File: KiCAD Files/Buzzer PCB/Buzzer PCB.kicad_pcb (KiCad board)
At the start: 2 copper layers, 25.2 x 22.9 mm, 13 parts, among them J1 JST-PH Battery IN, J2 JST-PH Feather BAT OUT, J4 Feather D13, Q1 S8050, SW1 SS12D00G5

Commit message: V2 PCB done
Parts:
- C1: value 47-100uF -> 47-100uF ELEC
- C2: value 0.1uF -> 0.1uF CER
- J1, J2: footprint Connector_JST:JST_PH_S2B-PH-K_1x02_P2.00mm_Horizontal -> Connector_JST:JST_PH_B2B-PH-K_1x02_P2.00mm_Vertical
- moved SW1 2.08 mm to (105.9, 104.9)
- moved D1 1.71 mm to (90.8, 112.4)
- moved C2 1.56 mm to (105.7, 98.4)
- moved J1 1.49 mm to (94.5, 95.6), turned to 180 degrees
- moved J2 1.14 mm to (100.7, 95.6), turned to 180 degrees
- moved C1 0.78 mm to (101.4, 111.2), turned to 180 degrees
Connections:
- J1 pad 1: BAT_IN -> GND
- J1 pad 2: GND -> BAT_IN
- J2 pad 1: SW_BAT -> GND
- J2 pad 2: GND -> SW_BAT
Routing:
- net GND: track 63.1 -> 56.5 mm
- net BAT_IN: track 20.1 -> 17.6 mm
- net BUZZER_LOW: track 12.7 -> 13.4 mm

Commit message: two_sided
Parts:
- J1, J2: footprint Connector_JST:JST_PH_B2B-PH-K_1x02_P2.00mm_Vertical -> Connector_JST:JST_PH_S2B-PH-K_1x02_P2.00mm_Horizontal
- moved J4 31.3 mm to (107.0, 116.0), turned to 180 degrees
- moved H1 30.1 mm to (85.4, 114.7), turned to 180 degrees
- moved H2 26.7 mm to (85.4, 96.9), turned to 180 degrees
- moved R1 24.0 mm to (106.9, 110.3), turned to 90 degrees
- moved C2 22.1 mm to (87.2, 110.4), turned to 0 degrees
- moved R2 19.8 mm to (104.4, 110.3), turned to -90 degrees
- moved D1 19.6 mm to (102.1, 96.4), turned to 0 degrees
- moved SW1 19.0 mm to (87.0, 103.9), turned to 90 degrees
- moved J2 18.7 mm to (93.2, 112.7), turned to 0 degrees
- moved J1 17.8 mm to (99.4, 112.7), turned to 0 degrees
- moved Q1 17.8 mm to (104.9, 101.6), turned to 90 degrees
- moved C1 16.8 mm to (91.5, 97.6), turned to 0 degrees
- moved BZ1 0.71 mm to (96.9, 104.1), turned to 0 degrees
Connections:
- J1 pad 1: GND -> BAT_IN
- J1 pad 2: BAT_IN -> GND
- J2 pad 1: GND -> SW_BAT
- J2 pad 2: SW_BAT -> GND
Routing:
- net D13: track 1.90 -> 6.42 mm, vias 0 -> 1
- net SW_BAT: track 48.2 -> 44.5 mm
- net BAT_IN: track 17.6 -> 14.4 mm
- net GND: track 56.5 -> 59.0 mm
- net BUZZER_LOW: track 13.4 -> 12.7 mm
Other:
- outline, holes or cut-outs redrawn

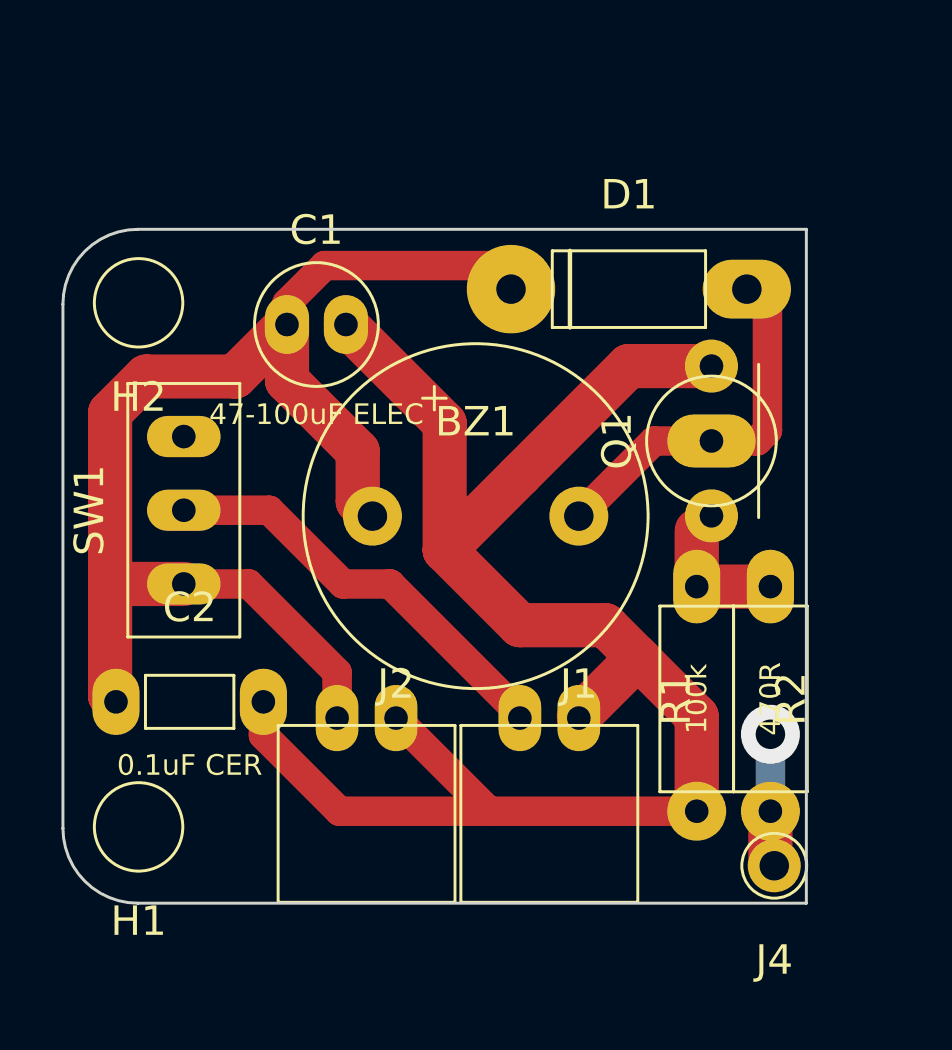
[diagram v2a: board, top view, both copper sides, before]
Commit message: Fix S8050 pinout and buzzer test interval
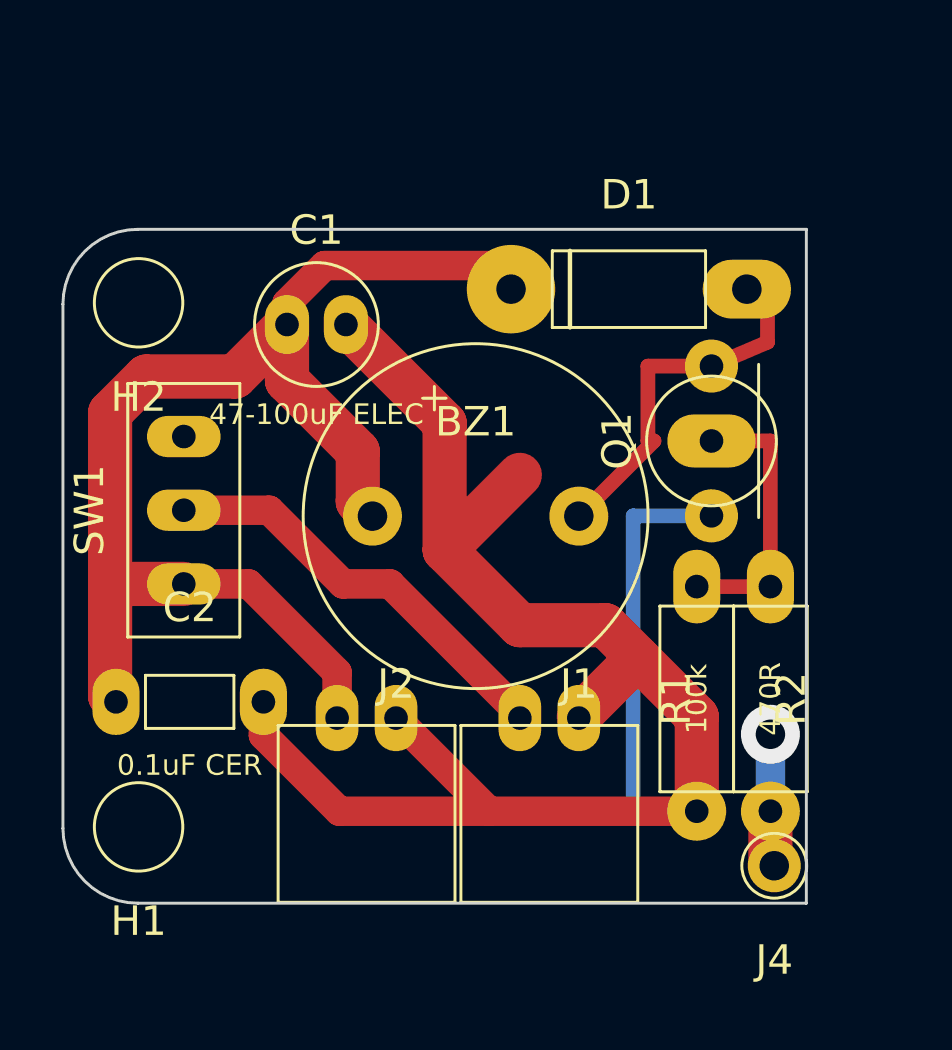
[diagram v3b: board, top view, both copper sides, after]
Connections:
- Q1 pad 1: BUZZER_BASE -> GND
- Q1 pad 2: BUZZER_LOW -> BUZZER_BASE
- Q1 pad 3: GND -> BUZZER_LOW
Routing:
- net GND: track 59.0 -> 65.8 mm
- net BUZZER_BASE: track 5.11 -> 9.44 mm
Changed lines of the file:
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@@
 		(layer "F.Cu")
 		(at 104.856051 101.563949 90)
-		(descr "S8050 NPN TO-92, formed leads, 2.54mm pad pitch, BCE per schematic, 0.8mm drills")
+		(descr "S8050 NPN TO-92, formed leads, 2.54mm pad pitch, EBC pinout, 0.8mm drills")
 		(property "Reference" "Q1"
 			(at 0 -3.2 90)
@@
 			)
 		)
-		(property "Description" "S8050 NPN TO-92, formed leads, 2.54mm pad pitch, BCE per schematic, 0.8mm drills"
+		(property "Description" "S8050 NPN TO-92, formed leads, 2.54mm pad pitch, EBC pinout, 0.8mm drills"
 			(at 0 0 90)
 			(layer "F.Fab")
@@
 			(keep_end_layers no)
 			(zone_layer_connections)
-			(net "BUZZER_BASE")
-			(pinfunction "B")
+			(net "GND")
+			(pinfunction "E")
 			(pintype "passive")
 		)
@@
 			(keep_end_layers no)
 			(zone_layer_connections)
-			(net "BUZZER_LOW")
-			(pinfunction "C")
+			(net "BUZZER_BASE")
+			(pinfunction "B")
 			(pintype "passive")
 		)
@@
 			(keep_end_layers no)
 			(zone_layer_connections)
-			(net "GND")
-			(pinfunction "E")
+			(net "BUZZER_LOW")
+			(pinfunction "C")
 			(pintype "passive")
 		)
@@
 	)
 	(segment
-		(start 102.046051 99.023949)
-		(end 104.856051 99.023949)
-		(width 1.5)
-		(layer "F.Cu")
+		(start 104.856051 104.103949)
+		(end 102.2 104.103949)
+		(width 0.5)
+		(layer "B.Cu")
+		(net "GND")
+	)
+	(segment
+		(start 102.2 104.103949)
+		(end 102.2 114.123949)
+		(width 0.5)
+		(layer "B.Cu")
+		(net "GND")
+	)
+	(segment
+		(start 102.2 114.123949)
+		(end 104.356051 114.123949)
+		(width 0.5)
+		(layer "B.Cu")
 		(net "GND")
 	)
@@
 	)
 	(segment
-		(start 98.356051 102.713949)
-		(end 102.046051 99.023949)
-		(width 1.5)
-		(layer "F.Cu")
-		(net "GND")
-	)
-	(segment
-		(start 104.356051 106.503949)
-		(end 104.356051 104.603949)
-		(width 1.5)
+		(start 106.856051 106.503949)
+		(end 106.856051 101.563949)
+		(width 0.5)
 		(layer "F.Cu")
 		(net "BUZZER_BASE")
 	)
 	(segment
-		(start 104.356051 104.603949)
-		(end 104.856051 104.103949)
-		(width 1)
+		(start 106.856051 101.563949)
+		(end 104.856051 101.563949)
+		(width 0.5)
 		(layer "F.Cu")
 		(net "BUZZER_BASE")
@@
 		(start 106.856051 106.503949)
 		(end 104.356051 106.503949)
-		(width 1.5)
+		(width 0.5)
 		(layer "F.Cu")
 		(net "BUZZER_BASE")
@@
 	)
 	(segment
-		(start 106.406051 101.563949)
-		(end 104.856051 101.563949)
-		(width 1)
-		(layer "F.Cu")
-		(net "BUZZER_LOW")
-	)
-	(segment
 		(start 106.756051 97.113949)
-		(end 106.756051 101.213949)
-		(width 1)
+		(end 106.756051 98.213949)
+		(width 0.5)
 		(layer "F.Cu")
 		(net "BUZZER_LOW")
@@
 		(start 102.906051 101.563949)
 		(end 100.356051 104.113949)
-		(width 1)
+		(width 0.5)
 		(layer "F.Cu")
 		(net "BUZZER_LOW")
 	)
 	(segment
-		(start 104.856051 101.563949)
+		(start 104.856051 99.023949)
+		(end 102.7 99.023949)
+		(width 0.5)
+		(layer "F.Cu")
+		(net "BUZZER_LOW")
+	)
+	(segment
+		(start 102.7 99.023949)
+		(end 102.7 101.563949)
+		(width 0.5)
+		(layer "F.Cu")
+		(net "BUZZER_LOW")
+	)
+	(segment
+		(start 102.7 101.563949)
 		(end 102.906051 101.563949)
-		(width 1)
+		(width 0.5)
 		(layer "F.Cu")
 		(net "BUZZER_LOW")
@@
 		(start 106.056051 96.413949)
 		(end 106.756051 97.113949)
-		(width 1)
+		(width 0.5)
 		(layer "F.Cu")
 		(net "BUZZER_LOW")
 	)
 	(segment
-		(start 106.756051 101.213949)
-		(end 106.406051 101.563949)
-		(width 1)
+		(start 106.756051 98.213949)
+		(end 104.856051 99.023949)
+		(width 0.5)
 		(layer "F.Cu")
 		(net "BUZZER_LOW")

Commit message: Fixed transistor pins
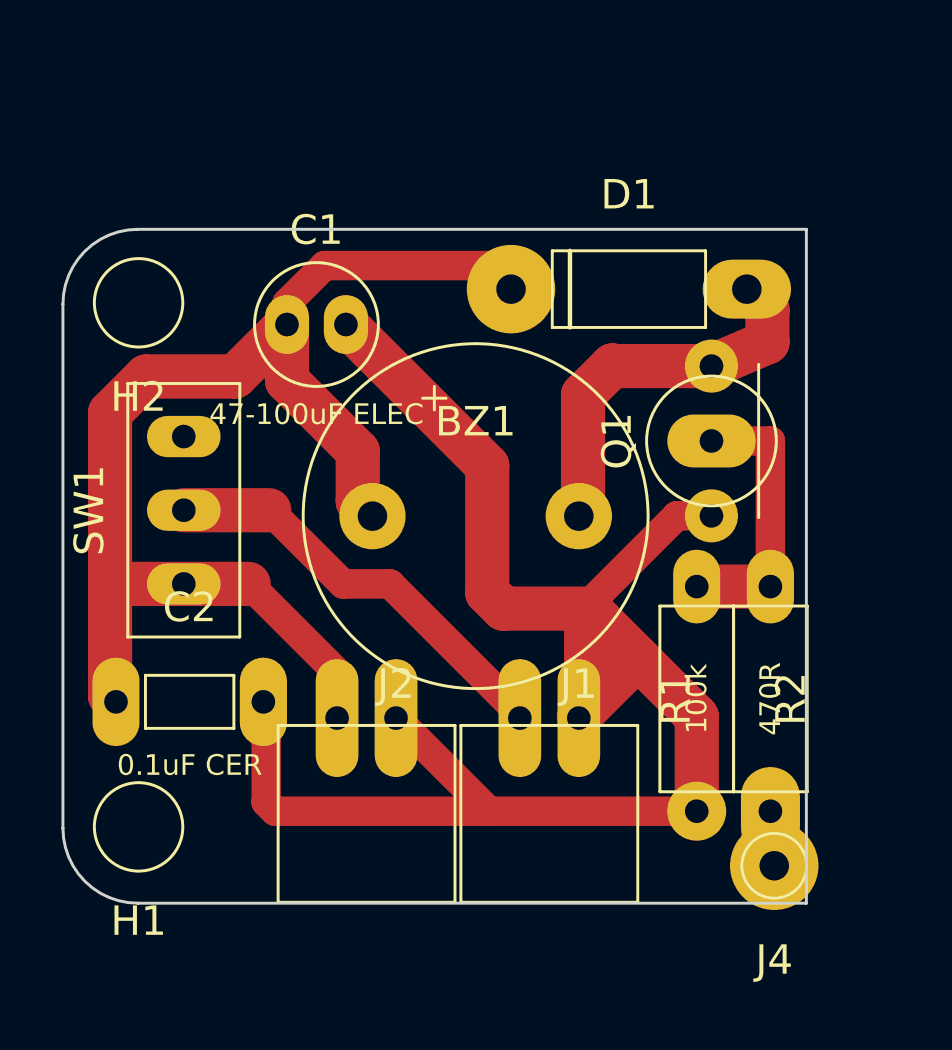
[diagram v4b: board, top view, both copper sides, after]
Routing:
- net GND: track 65.8 -> 59.8 mm
- net D13: track 6.42 -> 3.81 mm, vias 1 -> 0
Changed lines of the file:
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@@
 		(capping no)
 		(filling no)
-		(aux_axis_origin 85.422051 114.655349)
+		(aux_axis_origin 78.1 122.3)
 		(pcbplotparams
 			(layerselection 0x00000000_00000000_55555555_57555555)
@@
 			(layer "F.Fab")
 		)
-		(pad "1" thru_hole circle
+		(pad "e" thru_hole oval
 			(at 0 0 180)
-			(size 1.8 1.8)
+			(size 3 3)
 			(drill 1)
 			(layers "*.Cu" "F.Mask")
@@
 		(pad "1" thru_hole oval
 			(at -2.5 0)
-			(size 1.6 2.25)
+			(size 1.6 3)
 			(drill 0.8)
 			(layers "*.Cu" "F.Mask")
@@
 		(pad "2" thru_hole oval
 			(at 2.5 0)
-			(size 1.6 2.25)
+			(size 1.6 3)
 			(drill 0.8)
 			(layers "*.Cu" "F.Mask")
@@
 		(pad "1" thru_hole oval
 			(at -1 -1.75)
-			(size 1.45 2.25)
+			(size 1.45 4)
 			(drill 0.8)
 			(layers "*.Cu" "F.Mask")
@@
 		(pad "2" thru_hole oval
 			(at 1 -1.75)
-			(size 1.45 2.25)
+			(size 1.45 4)
 			(drill 0.8)
 			(layers "*.Cu" "F.Mask")
@@
 		(pad "1" thru_hole oval
 			(at -1 -1.75)
-			(size 1.45 2.25)
+			(size 1.45 4)
 			(drill 0.8)
 			(layers "*.Cu" "F.Mask")
@@
 		(pad "2" thru_hole oval
 			(at 1 -1.75)
-			(size 1.45 2.25)
+			(size 1.45 4)
 			(drill 0.8)
 			(layers "*.Cu" "F.Mask")
@@
 			(layer "F.Fab")
 		)
-		(pad "1" thru_hole circle
+		(pad "1" thru_hole oval
 			(at -3.81 0 90)
-			(size 2 2)
+			(size 3 2)
 			(drill 0.8)
 			(layers "*.Cu" "F.Mask")
@@
 		(pad "1" thru_hole circle
 			(at -3.5 0)
-			(size 2 2)
+			(size 2.25 2.25)
 			(drill 1)
 			(layers "*.Cu" "F.Mask")
@@
 		(pad "2" thru_hole circle
 			(at 3.5 0)
-			(size 2 2)
+			(size 2.25 2.25)
 			(drill 1)
 			(layers "*.Cu" "F.Mask")
@@
 		(start 106.856051 114.123949)
 		(end 106.856051 115.843949)
-		(width 1.5)
+		(width 2)
 		(layer "F.Cu")
 		(net "D13")
@@
 		(net "D13")
 	)
-	(via
-		(at 106.856051 111.513949)
-		(size 2)
-		(drill 1)
-		(layers "F.Cu" "B.Cu")
-		(free yes)
-		(net "D13")
-	)
 	(segment
 		(start 106.986051 114.253949)
@@
 	)
 	(segment
-		(start 106.856051 114.123949)
-		(end 106.856051 111.513949)
+		(start 106.986051 115.973949)
+		(end 106.986051 114.253949)
 		(width 1)
 		(layer "B.Cu")
@@
 	)
 	(segment
-		(start 106.986051 115.973949)
-		(end 106.986051 114.253949)
-		(width 1)
-		(layer "B.Cu")
-		(net "D13")
-	)
-	(segment
 		(start 91.731177 95.613949)
 		(end 90.456051 96.889075)
@@
 		(start 89.156051 106.413949)
 		(end 86.956051 106.413949)
-		(width 1)
+		(width 1.5)
 		(layer "F.Cu")
 		(net "SW_BAT")
@@
 	)
 	(segment
-		(start 98.356051 107.813949)
-		(end 95.806051 105.263949)
-		(width 1.5)
+		(start 92.456051 97.613949)
+		(end 97.25 102.407898)
+		(width 1.5)
+		(layer "F.Cu")
+		(net "GND")
+	)
+	(segment
+		(start 89.656051 111.545319)
+		(end 89.75 111.639268)
+		(width 1)
+		(layer "F.Cu")
+		(net "GND")
+	)
+	(segment
+		(start 100.692102 107.089873)
+		(end 100.692102 107.25)
+		(width 1)
 		(layer "F.Cu")
 		(net "GND")
@@
 	)
 	(segment
-		(start 102.356051 108.913949)
-		(end 101.256051 107.813949)
-		(width 1.5)
-		(layer "F.Cu")
-		(net "GND")
-	)
-	(segment
-		(start 100.356051 110.913949)
+		(start 100.692102 107.25)
 		(end 102.356051 108.913949)
 		(width 1.5)
@@
 	)
 	(segment
-		(start 95.806051 105.263949)
-		(end 98.356051 102.713949)
-		(width 1.5)
+		(start 89.75 113.819634)
+		(end 90.054315 114.123949)
+		(width 1)
+		(layer "F.Cu")
+		(net "GND")
+	)
+	(segment
+		(start 100.356051 107.586051)
+		(end 100.356051 108.75)
+		(width 1)
+		(layer "F.Cu")
+		(net "GND")
+	)
+	(segment
+		(start 89.75 111.639268)
+		(end 89.75 113.819634)
+		(width 1)
+		(layer "F.Cu")
+		(net "GND")
+	)
+	(segment
+		(start 100.692102 107.25)
+		(end 100.356051 107.586051)
+		(width 1)
+		(layer "F.Cu")
+		(net "GND")
+	)
+	(segment
+		(start 97.25 102.407898)
+		(end 97.25 106.707898)
+		(width 1.5)
+		(layer "F.Cu")
+		(net "GND")
+	)
+	(segment
+		(start 97.25 106.707898)
+		(end 97.792102 107.25)
+		(width 1.5)
+		(layer "F.Cu")
+		(net "GND")
+	)
+	(segment
+		(start 101.76 109.51)
+		(end 102.356051 108.913949)
+		(width 1.5)
+		(layer "F.Cu")
+		(net "GND")
+	)
+	(segment
+		(start 100.356051 108.75)
+		(end 101 108.75)
+		(width 1)
 		(layer "F.Cu")
 		(net "GND")
@@
 	)
 	(segment
+		(start 94.156051 110.963949)
+		(end 97.316051 114.123949)
+		(width 1)
+		(layer "F.Cu")
+		(net "GND")
+	)
+	(segment
+		(start 104.356051 114.123949)
+		(end 104.356051 110.913949)
+		(width 1.5)
+		(layer "F.Cu")
+		(net "GND")
+	)
+	(segment
+		(start 100.356051 108.75)
+		(end 100.356051 110.963949)
+		(width 1)
+		(layer "F.Cu")
+		(net "GND")
+	)
+	(segment
+		(start 90.054315 114.123949)
+		(end 97.316051 114.123949)
+		(width 1)
+		(layer "F.Cu")
+		(net "GND")
+	)
+	(segment
+		(start 101 108.75)
+		(end 101.76 109.51)
+		(width 1)
+		(layer "F.Cu")
+		(net "GND")
+	)
+	(segment
+		(start 103.678026 104.103949)
+		(end 100.692102 107.089873)
+		(width 1)
+		(layer "F.Cu")
+		(net "GND")
+	)
+	(segment
+		(start 97.792102 107.25)
+		(end 100.692102 107.25)
+		(width 1.5)
+		(layer "F.Cu")
+		(net "GND")
+	)
+	(segment
+		(start 104.856051 104.103949)
+		(end 103.678026 104.103949)
+		(width 1)
+		(layer "F.Cu")
+		(net "GND")
+	)
+	(segment
+		(start 100.356051 110.913949)
+		(end 101.76 109.51)
+		(width 1.5)
+		(layer "F.Cu")
+		(net "GND")
+	)
+	(segment
 		(start 89.656051 110.413949)
 		(end 89.656051 111.545319)
@@
 	)
 	(segment
-		(start 94.156051 110.963949)
-		(end 97.316051 114.123949)
-		(width 1)
-		(layer "F.Cu")
-		(net "GND")
-	)
-	(segment
-		(start 104.356051 114.123949)
-		(end 104.356051 110.913949)
-		(width 1.5)
-		(layer "F.Cu")
-		(net "GND")
-	)
-	(segment
-		(start 89.656051 111.545319)
-		(end 92.234681 114.123949)
-		(width 1)
-		(layer "F.Cu")
-		(net "GND")
-	)
-	(segment
-		(start 92.234681 114.123949)
-		(end 97.316051 114.123949)
-		(width 1)
-		(layer "F.Cu")
-		(net "GND")
-	)
-	(segment
-		(start 95.806051 100.963949)
-		(end 95.806051 105.263949)
-		(width 1.5)
-		(layer "F.Cu")
-		(net "GND")
-	)
-	(segment
-		(start 92.456051 97.613949)
-		(end 95.806051 100.963949)
-		(width 1.5)
-		(layer "F.Cu")
-		(net "GND")
-	)
-	(segment
-		(start 104.856051 104.103949)
-		(end 102.2 104.103949)
-		(width 0.5)
-		(layer "B.Cu")
-		(net "GND")
-	)
-	(segment
-		(start 102.2 104.103949)
-		(end 102.2 114.123949)
-		(width 0.5)
-		(layer "B.Cu")
-		(net "GND")
-	)
-	(segment
-		(start 102.2 114.123949)
-		(end 104.356051 114.123949)
-		(width 0.5)
-		(layer "B.Cu")
-		(net "GND")
-	)
-	(segment
-		(start 101.256051 107.813949)
-		(end 98.356051 107.813949)
-		(width 1.5)
-		(layer "F.Cu")
-		(net "GND")
-	)
-	(segment
 		(start 104.356051 110.913949)
 		(end 102.356051 108.913949)
@@
 		(start 106.856051 106.503949)
 		(end 106.856051 101.563949)
-		(width 0.5)
+		(width 1)
 		(layer "F.Cu")
 		(net "BUZZER_BASE")
@@
 		(start 106.856051 101.563949)
 		(end 104.856051 101.563949)
-		(width 0.5)
+		(width 1)
 		(layer "F.Cu")
 		(net "BUZZER_BASE")
@@
 		(start 106.856051 106.503949)
 		(end 104.356051 106.503949)
-		(width 0.5)
+		(width 1.5)
 		(layer "F.Cu")
 		(net "BUZZER_BASE")
@@
 		(start 89.856051 103.913949)
 		(end 86.956051 103.913949)
-		(width 1)
+		(width 1.5)
 		(layer "F.Cu")
 		(net "BAT_IN")
@@
 		(start 106.756051 97.113949)
 		(end 106.756051 98.213949)
-		(width 0.5)
+		(width 1.5)
 		(layer "F.Cu")
 		(net "BUZZER_LOW")
 	)
 	(segment
-		(start 102.906051 101.563949)
+		(start 100.5 100)
+		(end 100.5 103.97)
+		(width 1.5)
+		(layer "F.Cu")
+		(net "BUZZER_LOW")
+	)
+	(segment
+		(start 104.856051 99.023949)
+		(end 101.523949 99.023949)
+		(width 1.5)
+		(layer "F.Cu")
+		(net "BUZZER_LOW")
+	)
+	(segment
+		(start 101.5 99)
+		(end 100.5 100)
+		(width 1.5)
+		(layer "F.Cu")
+		(net "BUZZER_LOW")
+	)
+	(segment
+		(start 100.5 103.97)
 		(end 100.356051 104.113949)
-		(width 0.5)
-		(layer "F.Cu")
-		(net "BUZZER_LOW")
-	)
-	(segment
-		(start 104.856051 99.023949)
-		(end 102.7 99.023949)
-		(width 0.5)
-		(layer "F.Cu")
-		(net "BUZZER_LOW")
-	)
-	(segment
-		(start 102.7 99.023949)
-		(end 102.7 101.563949)
-		(width 0.5)
-		(layer "F.Cu")
-		(net "BUZZER_LOW")
-	)
-	(segment
-		(start 102.7 101.563949)
-		(end 102.906051 101.563949)
-		(width 0.5)
+		(width 1.5)
 		(layer "F.Cu")
 		(net "BUZZER_LOW")
@@
 		(start 106.056051 96.413949)
 		(end 106.756051 97.113949)
-		(width 0.5)
+		(width 1.5)
 		(layer "F.Cu")
 		(net "BUZZER_LOW")
@@
 		(start 106.756051 98.213949)
 		(end 104.856051 99.023949)
-		(width 0.5)
+		(width 1.5)
 		(layer "F.Cu")
 		(net "BUZZER_LOW")
+	)
+	(segment
+		(start 101.523949 99.023949)
+		(end 101.5 99)
+		(width 1.5)
+		(layer "F.Cu")
+		(net "BUZZER_LOW")
